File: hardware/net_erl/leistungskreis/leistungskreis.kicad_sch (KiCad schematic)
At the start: 15 parts, among them J1 Co_5xV, J5 Co_x3, J8 Co_x31, K2 HF46F_005-HS1, Q1 FQP27P06, U2 PC817

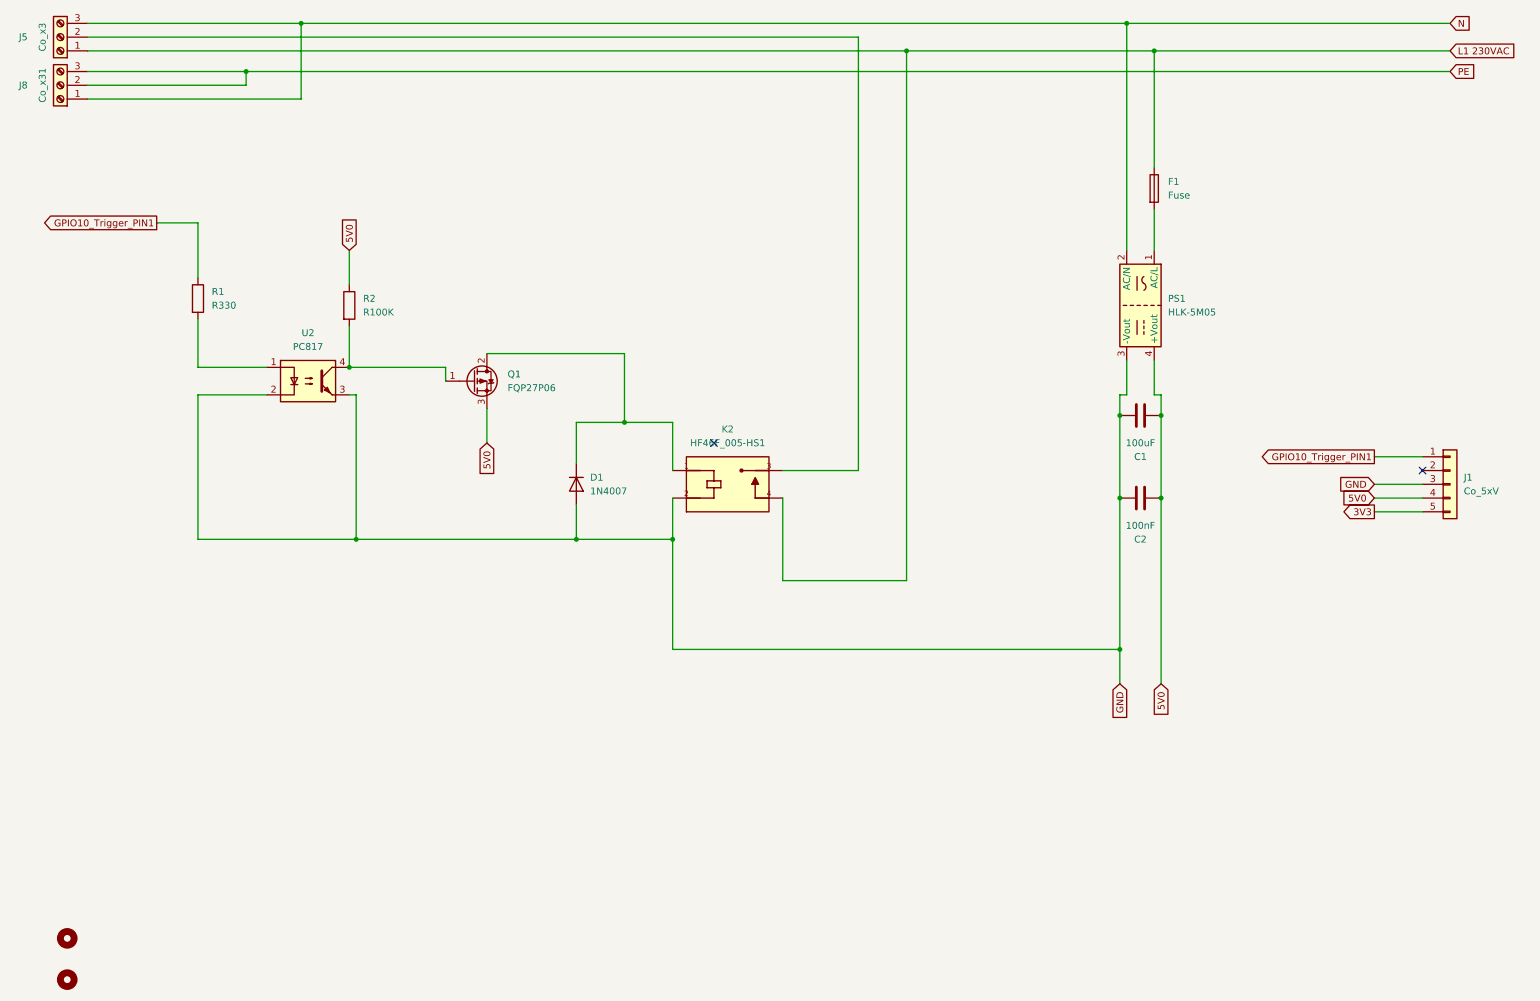
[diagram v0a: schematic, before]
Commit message: fix: server_contract_smoke.ps1 - process.argv.slice(1)->slice(2)
- Bug: node -e schiebt das eval-Skript als argv[1], Argumente starten erst bei argv[2]
- slice(1) inkludierte das Skript als deviceId → DB-Check schlug immer fehl
- Fix: slice(2) korrekt
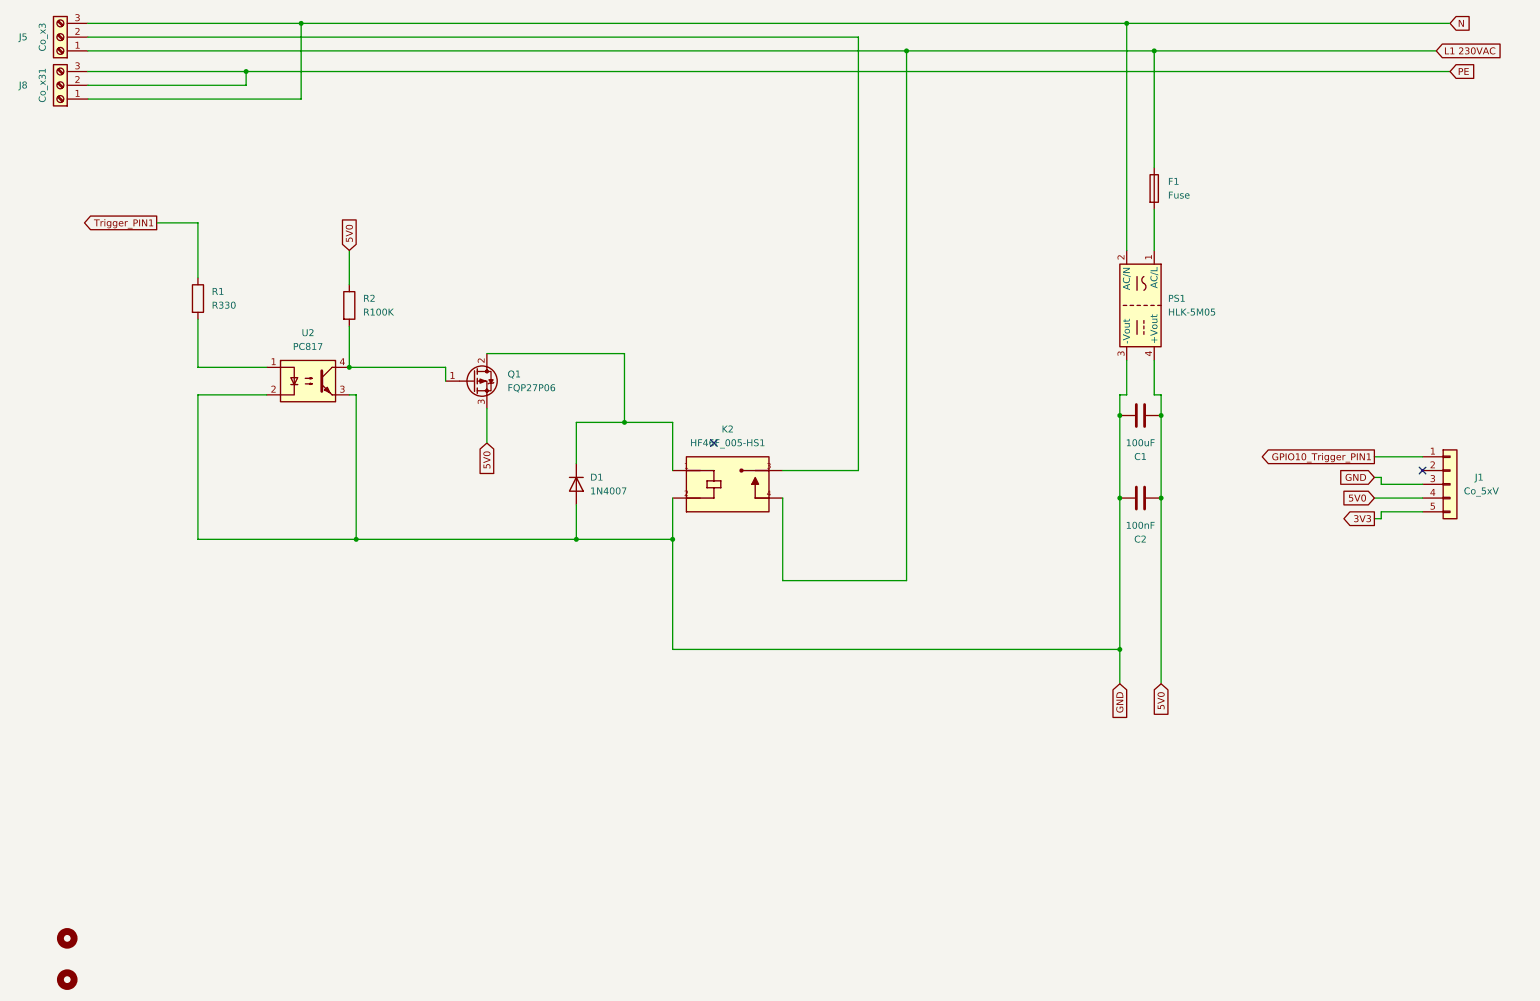
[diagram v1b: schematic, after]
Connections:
- net GPIO10_Trigger_PIN1: no longer R1.1
- new net Trigger_PIN1: R1.1
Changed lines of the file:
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@@
 	(wire
 		(pts
-			(xy 219.71 20.32) (xy 274.32 20.32)
+			(xy 219.71 20.32) (xy 271.78 20.32)
 		)
 		(stroke
@@
 	(wire
 		(pts
-			(xy 260.35 100.33) (xy 269.24 100.33)
+			(xy 260.35 99.06) (xy 261.62 99.06)
 		)
 		(stroke
@@
 	(wire
 		(pts
+			(xy 261.62 100.33) (xy 269.24 100.33)
+		)
+		(stroke
+			(width 0)
+			(type default)
+		)
+	)
+	(wire
+		(pts
 			(xy 35.56 52.07) (xy 43.18 52.07)
 		)
@@
 	(wire
 		(pts
-			(xy 260.35 105.41) (xy 269.24 105.41)
+			(xy 260.35 106.68) (xy 261.62 106.68)
 		)
 		(stroke
@@
 	(wire
 		(pts
+			(xy 261.62 105.41) (xy 269.24 105.41)
+		)
+		(stroke
+			(width 0)
+			(type default)
+		)
+	)
+	(wire
+		(pts
 			(xy 43.18 52.07) (xy 43.18 62.23)
 		)
@@
 	(wire
 		(pts
+			(xy 261.62 106.68) (xy 261.62 105.41)
+		)
+		(stroke
+			(width 0)
+			(type default)
+		)
+	)
+	(wire
+		(pts
 			(xy 113.03 88.9) (xy 113.03 96.52)
 		)
@@
 		(pts
 			(xy 173.99 20.32) (xy 219.71 20.32)
+		)
+		(stroke
+			(width 0)
+			(type default)
+		)
+	)
+	(wire
+		(pts
+			(xy 261.62 99.06) (xy 261.62 100.33)
 		)
 		(stroke
@@
 		)
 	)
-	(global_label "GPIO10_Trigger_PIN1"
+	(global_label "Trigger_PIN1"
 		(shape output)
 		(at 35.56 52.07 180)
@@
 		)
 		(property "Intersheetrefs" "${INTERSHEET_REFS}"
-			(at 12.7991 52.07 0)
+			(at 20.661 52.07 0)
 			(effects
 				(font
@@
 	(global_label "GND"
 		(shape input)
-		(at 260.35 100.33 180)
+		(at 260.35 99.06 180)
 		(fields_autoplaced yes)
 		(effects
@@
 		)
 		(property "Intersheetrefs" "${INTERSHEET_REFS}"
-			(at 253.4943 100.33 0)
+			(at 253.4943 99.06 0)
 			(effects
 				(font
@@
 	(global_label "L1 230VAC"
 		(shape input)
-		(at 274.32 20.32 0)
+		(at 271.78 20.32 0)
 		(fields_autoplaced yes)
 		(effects
@@
 		)
 		(property "Intersheetrefs" "${INTERSHEET_REFS}"
-			(at 287.5861 20.32 0)
+			(at 285.0461 20.32 0)
 			(effects
 				(font
@@
 	(global_label "3V3"
 		(shape output)
-		(at 260.35 105.41 180)
+		(at 260.35 106.68 180)
 		(fields_autoplaced yes)
 		(effects
@@
 		)
 		(property "Intersheetrefs" "${INTERSHEET_REFS}"
-			(at 253.8572 105.41 0)
+			(at 253.8572 106.68 0)
 			(effects
 				(font
@@
 		(on_board yes)
 		(dnp no)
-		(fields_autoplaced yes)
 		(property "Reference" "J1"
-			(at 276.86 99.0599 0)
-			(effects
-				(font
+			(at 278.892 99.06 0)
+			(effects
+				(font
